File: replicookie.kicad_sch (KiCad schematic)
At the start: 0 parts

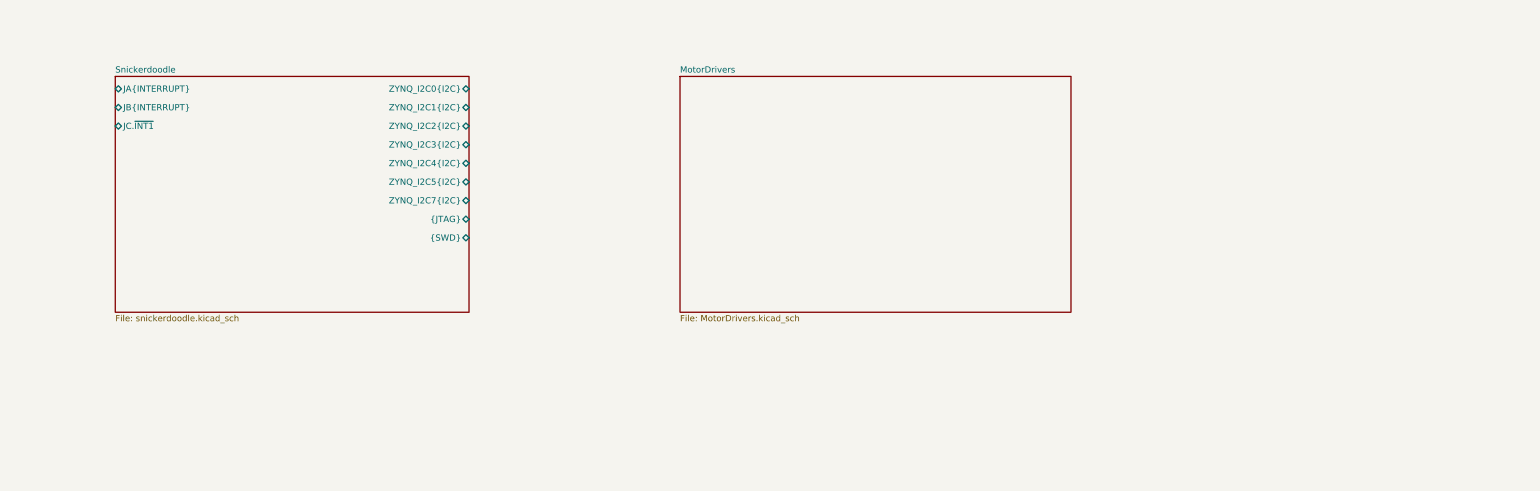
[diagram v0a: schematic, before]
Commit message: Increase text size, redo bus labels
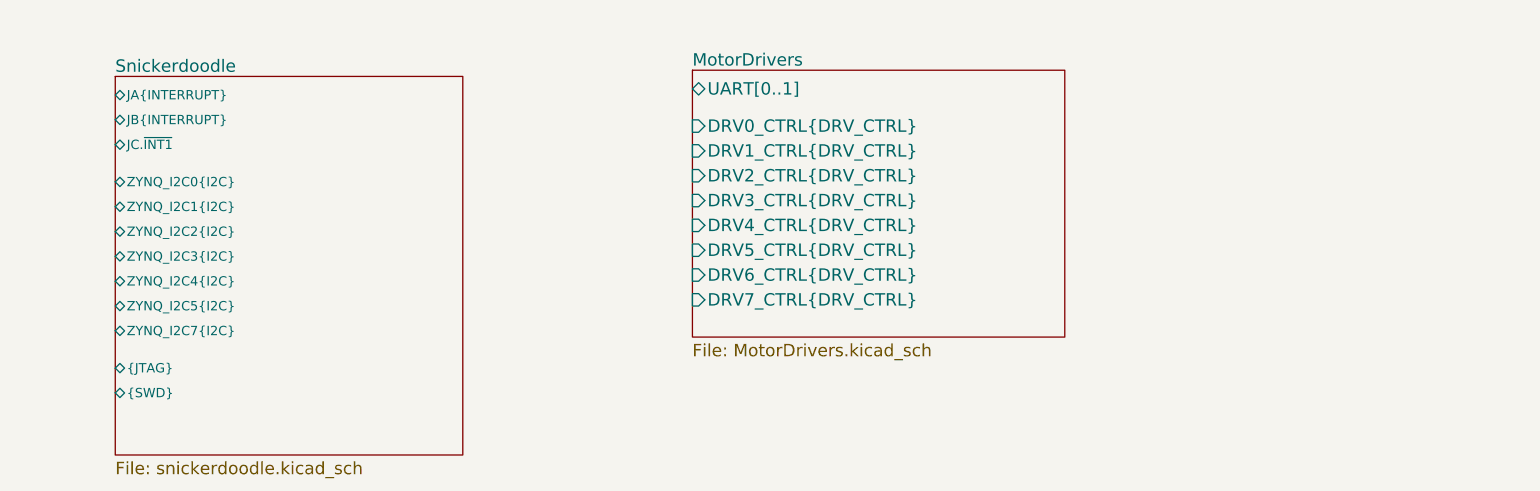
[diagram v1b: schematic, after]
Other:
- sheet MotorDrivers ports: added DRV0_CTRL{DRV_CTRL}, DRV1_CTRL{DRV_CTRL}, DRV2_CTRL{DRV_CTRL}, DRV3_CTRL{DRV_CTRL}, DRV4_CTRL{DRV_CTRL}, DRV5_CTRL{DRV_CTRL}, DRV6_CTRL{DRV_CTRL}, DRV7_CTRL{DRV_CTRL}, UART[0..1]; removed none

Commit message: Add RTC
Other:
- added sheet RealTimeClock (RTC.kicad_sch)
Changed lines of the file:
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@@
 (kicad_sch (version 20200608) (host eeschema "5.99.0-unknown-e376750~101~ubuntu20.04.1")
-  (page 1 11)
+  (page 1 12)
   (paper "B")
   (title_block
@@
     (comment 1 "Drawn by: Cameron McQuinn")
   )
-  (sheet (at 203.2 63.5) (size 76.2 54.61)
+  (bus (pts (xy 101.6 69.85) (xy 127 69.85))
+    (stroke (width 0) (type solid) (color 0 0 0 0))
+  )
+  (bus (pts (xy 127 69.85) (xy 127 80.01))
+    (stroke (width 0) (type solid) (color 0 0 0 0))
+  )
+  (bus (pts (xy 127 80.01) (xy 180.34 80.01))
+    (stroke (width 0) (type solid) (color 0 0 0 0))
+  )
+  (sheet (at 298.45 58.42) (size 76.2 54.61)
     (stroke (width 0.0006) (type solid) (color 132 0 132 1))
     (fill (color 255 255 255 0.0000))
-    (property "Sheet name" "MotorDrivers" (id 0) (at 203.2 62.8643 0)
+    (property "Sheet name" "MotorDrivers" (id 0) (at 298.45 57.7843 0)
       (effects (font (size 2.54 2.54)) (justify left bottom))
     )
-    (property "Sheet file" "MotorDrivers.kicad_sch" (id 1) (at 203.2 119.38 0)
+    (property "Sheet file" "MotorDrivers.kicad_sch" (id 1) (at 298.45 114.3 0)
       (effects (font (size 2.54 2.54)) (justify left top))
     )
-    (pin "DRV5_CTRL{DRV_CTRL}" input (at 203.2 100.33 180)
+    (pin "DRV5_CTRL{DRV_CTRL}" input (at 298.45 95.25 180)
       (effects (font (size 2.54 2.54)) (justify left))
     )
-    (pin "DRV6_CTRL{DRV_CTRL}" input (at 203.2 105.41 180)
+    (pin "DRV6_CTRL{DRV_CTRL}" input (at 298.45 100.33 180)
       (effects (font (size 2.54 2.54)) (justify left))
     )
-    (pin "DRV7_CTRL{DRV_CTRL}" input (at 203.2 110.49 180)
+    (pin "DRV7_CTRL{DRV_CTRL}" input (at 298.45 105.41 180)
       (effects (font (size 2.54 2.54)) (justify left))
     )
-    (pin "DRV4_CTRL{DRV_CTRL}" input (at 203.2 95.25 180)
+    (pin "DRV4_CTRL{DRV_CTRL}" input (at 298.45 90.17 180)
       (effects (font (size 2.54 2.54)) (justify left))
     )
-    (pin "DRV0_CTRL{DRV_CTRL}" input (at 203.2 74.93 180)
+    (pin "DRV0_CTRL{DRV_CTRL}" input (at 298.45 69.85 180)
       (effects (font (size 2.54 2.54)) (justify left))
     )
-    (pin "DRV1_CTRL{DRV_CTRL}" input (at 203.2 80.01 180)
+    (pin "DRV1_CTRL{DRV_CTRL}" input (at 298.45 74.93 180)
       (effects (font (size 2.54 2.54)) (justify left))
     )
-    (pin "DRV2_CTRL{DRV_CTRL}" input (at 203.2 85.09 180)
+    (pin "DRV2_CTRL{DRV_CTRL}" input (at 298.45 80.01 180)
       (effects (font (size 2.54 2.54)) (justify left))
     )
-    (pin "DRV3_CTRL{DRV_CTRL}" input (at 203.2 90.17 180)
+    (pin "DRV3_CTRL{DRV_CTRL}" input (at 298.45 85.09 180)
       (effects (font (size 2.54 2.54)) (justify left))
     )
-    (pin "UART[0..1]" bidirectional (at 203.2 67.31 180)
+    (pin "UART[0..1]" bidirectional (at 298.45 62.23 180)
       (effects (font (size 2.54 2.54)) (justify left))
     )
   )
-  (sheet (at 85.09 64.77) (size 71.12 77.47)
+  (sheet (at 63.5 63.5) (size 38.1 12.7)
+    (stroke (width 0.0006) (type solid) (color 132 0 132 1))
+    (fill (color 255 255 255 0.0000))
+    (property "Sheet name" "RealTimeClock" (id 0) (at 63.5 62.8643 0)
+      (effects (font (size 2.54 2.54)) (justify left bottom))
+    )
+    (property "Sheet file" "RTC.kicad_sch" (id 1) (at 63.5 77.47 0)
+      (effects (font (size 2.54 2.54)) (justify left top))
+    )
+    (pin "{I2C}" bidirectional (at 101.6 69.85 0)
+      (effects (font (size 2.54 2.54)) (justify right))
+    )
+  )
+  (sheet (at 180.34 58.42) (size 71.12 77.47)
     (stroke (width 0.001) (type solid) (color 132 0 132 1))
     (fill (color 255 255 255 0.0000))
-    (property "Sheet name" "Snickerdoodle" (id 0) (at 85.09 64.1341 0)
+    (property "Sheet name" "Snickerdoodle" (id 0) (at 180.34 57.7841 0)
       (effects (font (size 2.54 2.54)) (justify left bottom))
     )
-    (property "Sheet file" "snickerdoodle.kicad_sch" (id 1) (at 85.09 143.51 0)
+    (property "Sheet file" "snickerdoodle.kicad_sch" (id 1) (at 180.34 137.16 0)
       (effects (font (size 2.54 2.54)) (justify left top))
     )
-    (pin "ZYNQ_I2C2{I2C}" bidirectional (at 85.09 96.52 180)
-      (effects (font (size 1.905 1.905)) (justify left))
+    (pin "ZYNQ_I2C2{I2C}" bidirectional (at 180.34 90.17 180)
+      (effects (font (size 2.54 2.54)) (justify left))
     )
-    (pin "ZYNQ_I2C0{I2C}" bidirectional (at 85.09 86.36 180)
-      (effects (font (size 1.905 1.905)) (justify left))
+    (pin "ZYNQ_I2C0{I2C}" bidirectional (at 180.34 80.01 180)
+      (effects (font (size 2.54 2.54)) (justify left))
     )
-    (pin "ZYNQ_I2C3{I2C}" bidirectional (at 85.09 101.6 180)
-      (effects (font (size 1.905 1.905)) (justify left))
+    (pin "ZYNQ_I2C3{I2C}" bidirectional (at 180.34 95.25 180)
+      (effects (font (size 2.54 2.54)) (justify left))
     )
-    (pin "JB{INTERRUPT}" bidirectional (at 85.09 73.66 180)
-      (effects (font (size 1.905 1.905)) (justify left))
+    (pin "JB{INTERRUPT}" bidirectional (at 180.34 67.31 180)
+      (effects (font (size 2.54 2.54)) (justify left))
     )
-    (pin "ZYNQ_I2C1{I2C}" bidirectional (at 85.09 91.44 180)
-      (effects (font (size 1.905 1.905)) (justify left))
+    (pin "ZYNQ_I2C1{I2C}" bidirectional (at 180.34 85.09 180)
+      (effects (font (size 2.54 2.54)) (justify left))
     )
-    (pin "ZYNQ_I2C4{I2C}" bidirectional (at 85.09 106.68 180)
-      (effects (font (size 1.905 1.905)) (justify left))
+    (pin "ZYNQ_I2C4{I2C}" bidirectional (at 180.34 100.33 180)
+      (effects (font (size 2.54 2.54)) (justify left))
     )
-    (pin "JC.~INT1" bidirectional (at 85.09 78.74 180)
-      (effects (font (size 1.905 1.905)) (justify left))
+    (pin "JC.~INT1" bidirectional (at 180.34 72.39 180)
+      (effects (font (size 2.54 2.54)) (justify left))
     )
-    (pin "JA{INTERRUPT}" bidirectional (at 85.09 68.58 180)
-      (effects (font (size 1.905 1.905)) (justify left))
+    (pin "JA{INTERRUPT}" bidirectional (at 180.34 62.23 180)
+      (effects (font (size 2.54 2.54)) (justify left))
     )
-    (pin "{JTAG}" bidirectional (at 85.09 124.46 180)
-      (effects (font (size 1.905 1.905)) (justify left))
+    (pin "{JTAG}" bidirectional (at 180.34 118.11 180)
+      (effects (font (size 2.54 2.54)) (justify left))
     )
-    (pin "ZYNQ_I2C7{I2C}" bidirectional (at 85.09 116.84 180)
-      (effects (font (size 1.905 1.905)) (justify left))
+    (pin "ZYNQ_I2C7{I2C}" bidirectional (at 180.34 110.49 180)
+      (effects (font (size 2.54 2.54)) (justify left))
     )
-    (pin "{SWD}" bidirectional (at 85.09 129.54 180)
-      (effects (font (size 1.905 1.905)) (justify left))
+    (pin "{SWD}" bidirectional (at 180.34 123.19 180)
+      (effects (font (size 2.54 2.54)) (justify left))
     )
-    (pin "ZYNQ_I2C5{I2C}" bidirectional (at 85.09 111.76 180)
-      (effects (font (size 1.905 1.905)) (justify left))
+    (pin "ZYNQ_I2C5{I2C}" bidirectional (at 180.34 105.41 180)
+      (effects (font (size 2.54 2.54)) (justify left))
     )
   )
   (symbol_instances
+    (path "/655846c9-6d11-4b61-aecf-3ea94510aa57/1027f7b7-977e-47ad-94fa-f467e4046458"
+      (reference "#PWR?") (unit 1)
+    )
+    (path "/655846c9-6d11-4b61-aecf-3ea94510aa57/56ba9407-5604-4a1b-9d8d-0c7a599e6af5"
+      (reference "#PWR?") (unit 1)
+    )
+    (path "/655846c9-6d11-4b61-aecf-3ea94510aa57/c24bbcfc-dcee-47a6-b40a-4dd46b0dc7c2"
+      (reference "#PWR?") (unit 1)
+    )
+    (path "/655846c9-6d11-4b61-aecf-3ea94510aa57/7268b520-ebce-4430-bcb0-317284fc9884"
+      (reference "BT?") (unit 1)
+    )
+    (path "/655846c9-6d11-4b61-aecf-3ea94510aa57/c8644347-8f22-4036-98a5-dad5bdc18185"
+      (reference "R?") (unit 1)
+    )
+    (path "/655846c9-6d11-4b61-aecf-3ea94510aa57/e08035a2-868e-4d03-82c7-2e0d9ac66ea7"
+      (reference "R?") (unit 1)
+    )
+    (path "/655846c9-6d11-4b61-aecf-3ea94510aa57/800d348c-6970-4aa9-85bd-4c910b2833b8"
+      (reference "U?") (unit 1)
+    )
+    (path "/655846c9-6d11-4b61-aecf-3ea94510aa57/6f10f941-6ce1-4fae-b2ff-12e416793bdf"
+      (reference "Y?") (unit 1)
+    )
     (path "/a32a7713-aceb-431f-82b6-7899cc3ddd29/08fc91e0-d17b-4470-a036-ebc456aa575c"
       (reference "#PWR0101") (unit 1)

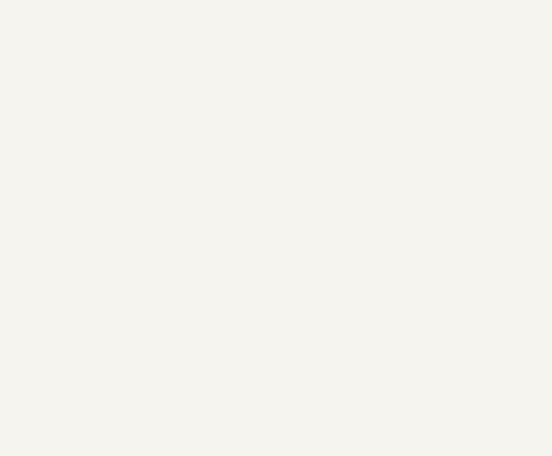
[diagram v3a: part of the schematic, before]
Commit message: Working on gigabit ethernet PHY
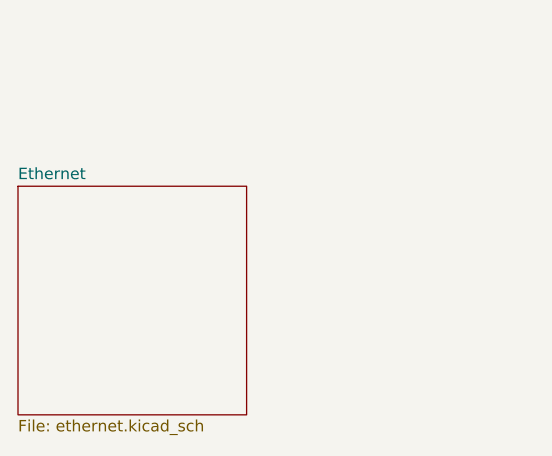
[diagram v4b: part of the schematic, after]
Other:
- added sheet Ethernet (ethernet.kicad_sch)
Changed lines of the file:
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@@
-(kicad_sch (version 20200608) (host eeschema "5.99.0-unknown-e376750~101~ubuntu20.04.1")
-  (page 1 12)
+(kicad_sch (version 20200618) (host eeschema "5.99.0-unknown-1463dd1~101~ubuntu20.04.1")
+  (page 1 13)
   (paper "B")
   (title_block
@@
   (bus (pts (xy 127 80.01) (xy 180.34 80.01))
     (stroke (width 0) (type solid) (color 0 0 0 0))
+  )
+  (sheet (at 63.5 114.3) (size 25.4 25.4)
+    (stroke (width 0.0006) (type solid) (color 132 0 132 1))
+    (fill (color 255 255 255 0.0000))
+    (property "Sheet name" "Ethernet" (id 0) (at 63.5 113.6643 0)
+      (effects (font (size 1.27 1.27)) (justify left bottom))
+    )
+    (property "Sheet file" "ethernet.kicad_sch" (id 1) (at 63.5 140.2087 0)
+      (effects (font (size 1.27 1.27)) (justify left top))
+    )
   )
   (sheet (at 298.45 58.42) (size 76.2 54.61)
@@
       (reference "Y?") (unit 1)
     )
+    (path "/0f4efdfd-e05f-4498-9f56-5655a2aa694e/09222420-deb1-47da-a89a-a3718e0688de"
+      (reference "#PWR?") (unit 1)
+    )
+    (path "/0f4efdfd-e05f-4498-9f56-5655a2aa694e/70345d75-85d1-4479-9289-63ff77194944"
+      (reference "#PWR?") (unit 1)
+    )
+    (path "/0f4efdfd-e05f-4498-9f56-5655a2aa694e/13bdc7de-f7bb-48f1-9393-7b9d24d49504"
+      (reference "C?") (unit 1)
+    )
+    (path "/0f4efdfd-e05f-4498-9f56-5655a2aa694e/33e8e6b1-e1b7-4192-a255-807159066929"
+      (reference "C?") (unit 1)
+    )
+    (path "/0f4efdfd-e05f-4498-9f56-5655a2aa694e/7977214e-6c23-4caa-aa76-899d91ac7923"
+      (reference "C?") (unit 1)
+    )
+    (path "/0f4efdfd-e05f-4498-9f56-5655a2aa694e/9c8266e8-a016-4a17-bd1b-2a315f6fa00f"
+      (reference "C?") (unit 1)
+    )
+    (path "/0f4efdfd-e05f-4498-9f56-5655a2aa694e/b89450ea-9e26-4f8f-95e1-826be3763bc1"
+      (reference "J?") (unit 1)
+    )
+    (path "/0f4efdfd-e05f-4498-9f56-5655a2aa694e/3cb0239e-f196-4d4d-af08-55a9ee357373"
+      (reference "U?") (unit 1)
+    )
+    (path "/0f4efdfd-e05f-4498-9f56-5655a2aa694e/a8dabf45-4912-4328-a436-c73a5b30f97c"
+      (reference "U?") (unit 1)
+    )
     (path "/a32a7713-aceb-431f-82b6-7899cc3ddd29/08fc91e0-d17b-4470-a036-ebc456aa575c"

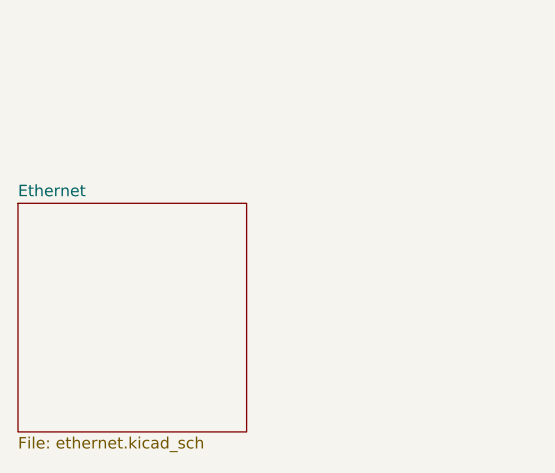
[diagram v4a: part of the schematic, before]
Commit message: WIre Ethernet PHY
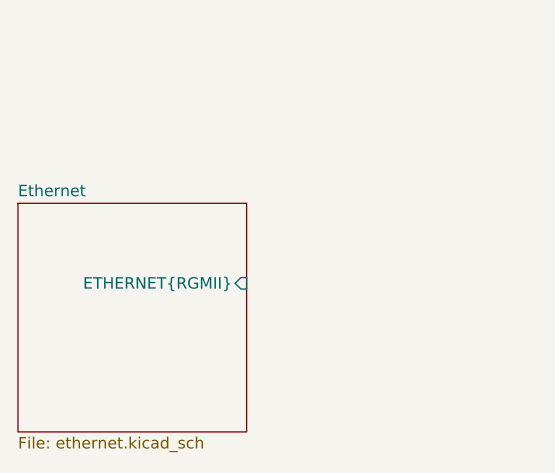
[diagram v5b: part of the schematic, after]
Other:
- sheet Ethernet ports: added ETHERNET{RGMII}; removed none
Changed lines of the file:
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@@
       (effects (font (size 1.27 1.27)) (justify left top))
+    )
+    (pin "ETHERNET{RGMII}" input (at 88.9 123.19 0)
+      (effects (font (size 1.27 1.27)) (justify right))
     )
   )
@@
       (reference "#PWR?") (unit 1)
     )
+    (path "/0f4efdfd-e05f-4498-9f56-5655a2aa694e/2d30443e-ede4-4ea9-9b89-5a939d944471"
+      (reference "#PWR?") (unit 1)
+    )
+    (path "/0f4efdfd-e05f-4498-9f56-5655a2aa694e/3bb89708-3d38-4329-9886-fae4d66e278a"
+      (reference "#PWR?") (unit 1)
+    )
+    (path "/0f4efdfd-e05f-4498-9f56-5655a2aa694e/4078494d-033f-48ae-b34c-9718e80e6cfd"
+      (reference "#PWR?") (unit 1)
+    )
+    (path "/0f4efdfd-e05f-4498-9f56-5655a2aa694e/41010021-f88f-4aac-8dd9-55ca71cb8c9d"
+      (reference "#PWR?") (unit 1)
+    )
+    (path "/0f4efdfd-e05f-4498-9f56-5655a2aa694e/6a04f952-859e-4d63-b76e-4e9dc95f6a1f"
+      (reference "#PWR?") (unit 1)
+    )
     (path "/0f4efdfd-e05f-4498-9f56-5655a2aa694e/70345d75-85d1-4479-9289-63ff77194944"
       (reference "#PWR?") (unit 1)
     )
+    (path "/0f4efdfd-e05f-4498-9f56-5655a2aa694e/7e72ad55-36e2-4fb0-a57a-99d77deb22eb"
+      (reference "#PWR?") (unit 1)
+    )
+    (path "/0f4efdfd-e05f-4498-9f56-5655a2aa694e/98516326-f946-4bc4-952d-0f718beabeb4"
+      (reference "#PWR?") (unit 1)
+    )
+    (path "/0f4efdfd-e05f-4498-9f56-5655a2aa694e/a283dacb-21fd-4baf-a93b-b64233060cdf"
+      (reference "#PWR?") (unit 1)
+    )
+    (path "/0f4efdfd-e05f-4498-9f56-5655a2aa694e/a58ca5ac-5d60-4059-828b-88d7c530baa2"
+      (reference "#PWR?") (unit 1)
+    )
+    (path "/0f4efdfd-e05f-4498-9f56-5655a2aa694e/aa4ca6c1-46be-4a07-9b77-7ed97a8fc9ca"
+      (reference "#PWR?") (unit 1)
+    )
+    (path "/0f4efdfd-e05f-4498-9f56-5655a2aa694e/ae3c03e5-e41f-4cd2-aaf9-f8314517f00d"
+      (reference "#PWR?") (unit 1)
+    )
+    (path "/0f4efdfd-e05f-4498-9f56-5655a2aa694e/c67c86f2-980d-4a8c-981b-5c7af3597dec"
+      (reference "#PWR?") (unit 1)
+    )
+    (path "/0f4efdfd-e05f-4498-9f56-5655a2aa694e/d105fb75-0982-4453-b7b0-fcb849848c26"
+      (reference "#PWR?") (unit 1)
+    )
+    (path "/0f4efdfd-e05f-4498-9f56-5655a2aa694e/d764c4e7-222e-4aed-b06c-1a1163743faa"
+      (reference "#PWR?") (unit 1)
+    )
+    (path "/0f4efdfd-e05f-4498-9f56-5655a2aa694e/ebc39279-0dbc-44d4-a8c6-89ae2555ca4d"
+      (reference "#PWR?") (unit 1)
+    )
+    (path "/0f4efdfd-e05f-4498-9f56-5655a2aa694e/fedd62a8-1eb1-4c6d-b171-810411e63b20"
+      (reference "#PWR?") (unit 1)
+    )
+    (path "/0f4efdfd-e05f-4498-9f56-5655a2aa694e/01413864-6964-470f-b6de-84b7889b8ac9"
+      (reference "C?") (unit 1)
+    )
+    (path "/0f4efdfd-e05f-4498-9f56-5655a2aa694e/080d322e-01df-4dda-a96f-ffcb8d79a261"
+      (reference "C?") (unit 1)
+    )
     (path "/0f4efdfd-e05f-4498-9f56-5655a2aa694e/13bdc7de-f7bb-48f1-9393-7b9d24d49504"
       (reference "C?") (unit 1)
     )
+    (path "/0f4efdfd-e05f-4498-9f56-5655a2aa694e/23834493-0234-47a7-b495-2bd00e782a12"
+      (reference "C?") (unit 1)
+    )
+    (path "/0f4efdfd-e05f-4498-9f56-5655a2aa694e/2537ddec-dda9-4646-b32f-9a87b53b8f7b"
+      (reference "C?") (unit 1)
+    )
     (path "/0f4efdfd-e05f-4498-9f56-5655a2aa694e/33e8e6b1-e1b7-4192-a255-807159066929"
       (reference "C?") (unit 1)
     )
+    (path "/0f4efdfd-e05f-4498-9f56-5655a2aa694e/45fbeb2e-cc1b-471b-95e7-1839edacf809"
+      (reference "C?") (unit 1)
+    )
+    (path "/0f4efdfd-e05f-4498-9f56-5655a2aa694e/5caedce4-0757-4b52-aa5e-dd26dde73d34"
+      (reference "C?") (unit 1)
+    )
     (path "/0f4efdfd-e05f-4498-9f56-5655a2aa694e/7977214e-6c23-4caa-aa76-899d91ac7923"
       (reference "C?") (unit 1)
     )
+    (path "/0f4efdfd-e05f-4498-9f56-5655a2aa694e/7be40d76-5c2e-4353-9562-edb7954796bc"
+      (reference "C?") (unit 1)
+    )
+    (path "/0f4efdfd-e05f-4498-9f56-5655a2aa694e/7c2eff58-2ed7-48cf-a407-bb081b00e51f"
+      (reference "C?") (unit 1)
+    )
+    (path "/0f4efdfd-e05f-4498-9f56-5655a2aa694e/871a1612-8927-4960-8bcf-4a510f7096db"
+      (reference "C?") (unit 1)
+    )
+    (path "/0f4efdfd-e05f-4498-9f56-5655a2aa694e/9b11854d-0375-4bc7-afb4-b3b62513d46f"
+      (reference "C?") (unit 1)
+    )
     (path "/0f4efdfd-e05f-4498-9f56-5655a2aa694e/9c8266e8-a016-4a17-bd1b-2a315f6fa00f"
       (reference "C?") (unit 1)
+    )
+    (path "/0f4efdfd-e05f-4498-9f56-5655a2aa694e/9cefe6e9-b378-4775-9e2e-6505a88d870a"
+      (reference "C?") (unit 1)
+    )
+    (path "/0f4efdfd-e05f-4498-9f56-5655a2aa694e/9f72085f-d88a-434c-9a2b-5b88d72a3ce3"
+      (reference "C?") (unit 1)
+    )
+    (path "/0f4efdfd-e05f-4498-9f56-5655a2aa694e/a41a30a7-3c00-4db9-945e-ded3cec11ac6"
+      (reference "C?") (unit 1)
+    )
+    (path "/0f4efdfd-e05f-4498-9f56-5655a2aa694e/aeb2a405-4d8a-46bc-88e9-b7482755f7ae"
+      (reference "C?") (unit 1)
+    )
+    (path "/0f4efdfd-e05f-4498-9f56-5655a2aa694e/bff1c475-b76b-4044-b5b7-1fac38ce5a12"
+      (reference "C?") (unit 1)
+    )
+    (path "/0f4efdfd-e05f-4498-9f56-5655a2aa694e/cccf06cd-0d1e-47d0-a000-742984337700"
+      (reference "C?") (unit 1)
+    )
+    (path "/0f4efdfd-e05f-4498-9f56-5655a2aa694e/d2af487d-e905-4ddb-9e9d-7478dbe6b01a"
+      (reference "C?") (unit 1)
+    )
+    (path "/0f4efdfd-e05f-4498-9f56-5655a2aa694e/d937e15d-a7c0-4683-9500-7fe3c4284e36"
+      (reference "C?") (unit 1)
+    )
+    (path "/0f4efdfd-e05f-4498-9f56-5655a2aa694e/dee3afe0-e38f-40c7-becd-2acbc543d12b"
+      (reference "C?") (unit 1)
+    )
+    (path "/0f4efdfd-e05f-4498-9f56-5655a2aa694e/f502381d-a128-41fc-9300-e4f5e07f3067"
+      (reference "C?") (unit 1)
+    )
+    (path "/0f4efdfd-e05f-4498-9f56-5655a2aa694e/317202c1-3641-4e5e-951f-ca05859dba00"
+      (reference "FB?") (unit 1)
+    )
+    (path "/0f4efdfd-e05f-4498-9f56-5655a2aa694e/990bdd0f-7edb-4c23-9189-702606cc1739"
+      (reference "FB?") (unit 1)
+    )
+    (path "/0f4efdfd-e05f-4498-9f56-5655a2aa694e/d9954e4f-8e1f-4f23-aabf-cce1e72a8c0e"
+      (reference "FB?") (unit 1)
     )
     (path "/0f4efdfd-e05f-4498-9f56-5655a2aa694e/b89450ea-9e26-4f8f-95e1-826be3763bc1"
       (reference "J?") (unit 1)
     )
+    (path "/0f4efdfd-e05f-4498-9f56-5655a2aa694e/e0a19686-4a92-4ed7-8007-55aad0a32852"
+      (reference "R?") (unit 1)
+    )
+    (path "/0f4efdfd-e05f-4498-9f56-5655a2aa694e/f3e79d2e-46ff-48e1-8293-b0cfa662ae8f"
+      (reference "R?") (unit 1)
+    )
+    (path "/0f4efdfd-e05f-4498-9f56-5655a2aa694e/296f1763-3d63-44b3-91f5-bef95ca6e078"
+      (reference "U?") (unit 1)
+    )
     (path "/0f4efdfd-e05f-4498-9f56-5655a2aa694e/3cb0239e-f196-4d4d-af08-55a9ee357373"
       (reference "U?") (unit 1)
     )
-    (path "/0f4efdfd-e05f-4498-9f56-5655a2aa694e/a8dabf45-4912-4328-a436-c73a5b30f97c"
-      (reference "U?") (unit 1)
+    (path "/0f4efdfd-e05f-4498-9f56-5655a2aa694e/28392559-6910-415c-87f3-862c9b428658"
+      (reference "X?") (unit 1)
     )
     (path "/a32a7713-aceb-431f-82b6-7899cc3ddd29/08fc91e0-d17b-4470-a036-ebc456aa575c"
